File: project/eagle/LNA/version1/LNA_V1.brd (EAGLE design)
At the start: 36.5 x 55.9 mm, 21 parts, among them Q1 MMBT3906LT1SMD, Q2 MMBT3906LT1SMD, Q3 SAV-541+, X1 SMA-142-0701-871/876, X2 SMA-142-0701-871/876

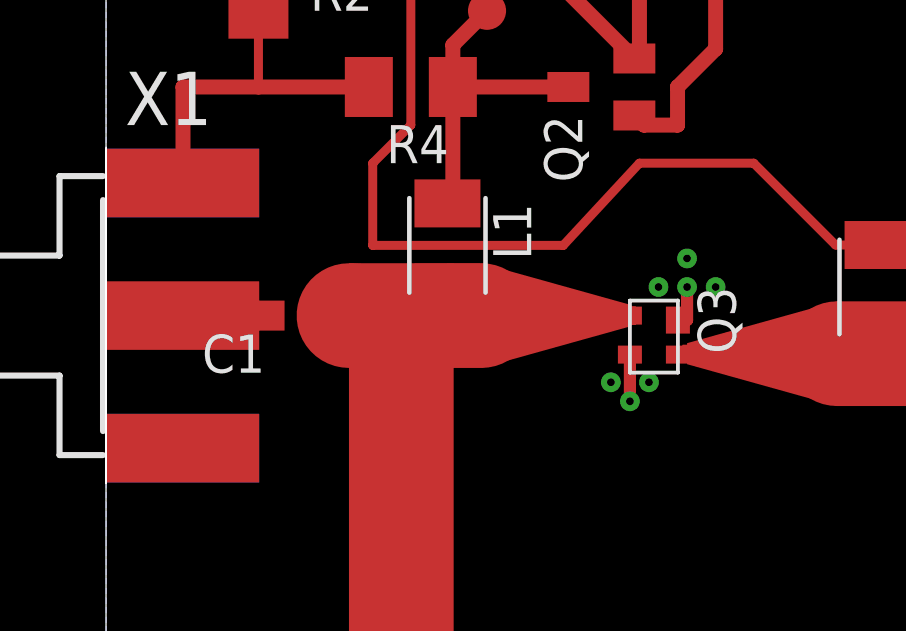
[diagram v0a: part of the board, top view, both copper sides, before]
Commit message: minor updates to layout, removed some vias
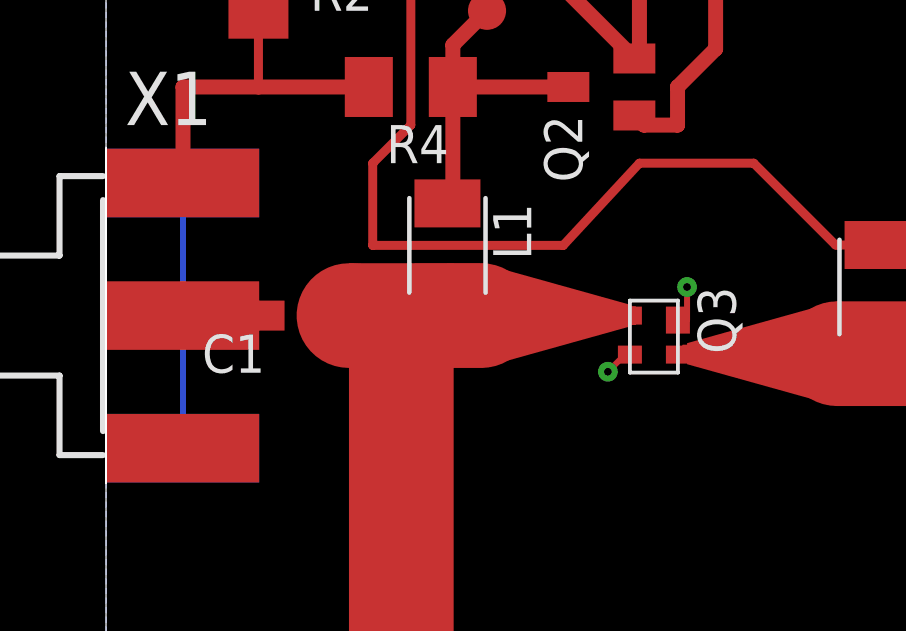
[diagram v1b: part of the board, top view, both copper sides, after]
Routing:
- net GND: track 14.8 -> 23.0 mm, vias 7 -> 2
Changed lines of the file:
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@@
 <setting verticaltext="up"/>
 </settings>
-<grid distance="0.05" unitdist="inch" unit="mm" style="lines" multiple="1" display="yes" altdistance="0.025" altunitdist="inch" altunit="inch"/>
+<grid distance="0.05" unitdist="mm" unit="mm" style="lines" multiple="1" display="yes" altdistance="0.025" altunitdist="inch" altunit="inch"/>
 <layers>
 <layer number="1" name="Top" color="4" fill="1" visible="yes" active="yes"/>
@@
 <wire x1="11.56" y1="26.8" x2="12.7" y2="27.94" width="0.5" layer="1"/>
 </signal>
-<signal name="GND" airwireshidden="yes">
+<signal name="GND">
 <contactref element="R3" pad="2"/>
 <contactref element="R4" pad="2"/>
@@
 </polygon>
 <wire x1="5.08" y1="27.81" x2="5.08" y2="25.4" width="0.3" layer="1"/>
-<wire x1="19.0625" y1="17.63" x2="19.3675" y2="17.63" width="0.4064" layer="1"/>
-<via x="19.3675" y="19.685" extent="1-16" drill="0.254"/>
-<via x="20.32" y="18.7325" extent="1-16" drill="0.254"/>
-<via x="18.415" y="18.7325" extent="1-16" drill="0.254"/>
 <via x="19.3675" y="18.7325" extent="1-16" drill="0.254"/>
-<via x="16.8275" y="15.5575" extent="1-16" drill="0.254"/>
-<via x="17.4625" y="14.9225" extent="1-16" drill="0.254"/>
-<via x="18.0975" y="15.5575" extent="1-16" drill="0.254"/>
-<wire x1="17.4625" y1="16.48" x2="17.4625" y2="14.9225" width="0.4064" layer="1"/>
-<wire x1="19.3675" y1="17.63" x2="19.3675" y2="18.7325" width="0.4064" layer="1"/>
+<via x="16.7275" y="15.9075" extent="1-16" drill="0.254"/>
+<wire x1="19.3675" y1="17.63" x2="19.3675" y2="18.7325" width="0.2" layer="1"/>
 <contactref element="X2" pad="G@1"/>
 <contactref element="X2" pad="G@2"/>
 <contactref element="X2" pad="G@3"/>
 <contactref element="X2" pad="G@4"/>
+<wire x1="17.4625" y1="16.48" x2="17.3" y2="16.48" width="0.2" layer="1"/>
+<wire x1="17.3" y1="16.48" x2="16.7275" y2="15.9075" width="0.2" layer="1"/>
+<wire x1="19.0625" y1="17.63" x2="19.3675" y2="17.63" width="0.2" layer="1"/>
+<wire x1="2.5654" y1="13.3604" x2="2.5654" y2="22.1996" width="0.2" layer="16"/>
 <wire x1="32.9946" y1="20.9296" x2="32.9946" y2="20.9296" width="0" layer="19" extent="1-16"/>
 <wire x1="32.9946" y1="12.0904" x2="32.9946" y2="12.0904" width="0" layer="19" extent="1-16"/>
